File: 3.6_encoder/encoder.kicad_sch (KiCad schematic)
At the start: 3 parts, among them M1 Motor_Servo, SW1 RotaryEncoder_Switch, U1 ESP32-S3-DevKitC

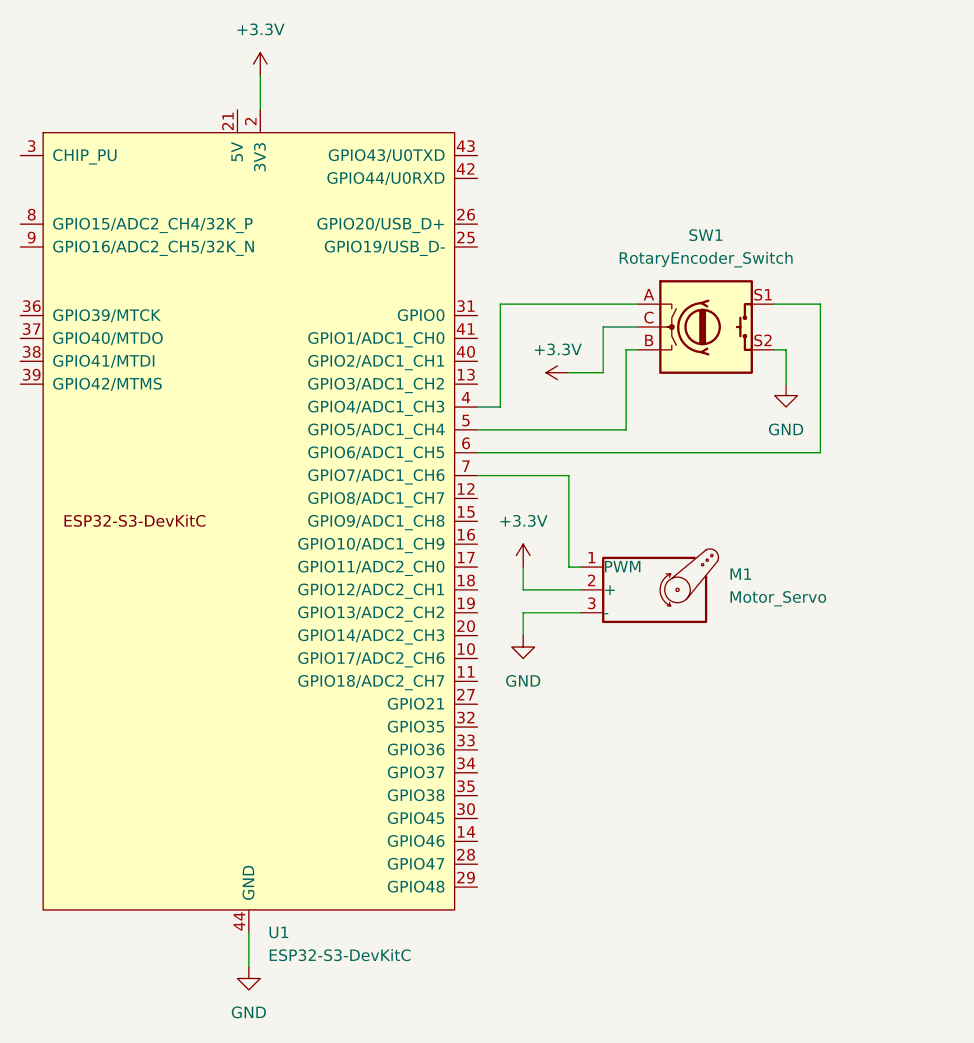
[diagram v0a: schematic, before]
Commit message: added parts for HW 3.6
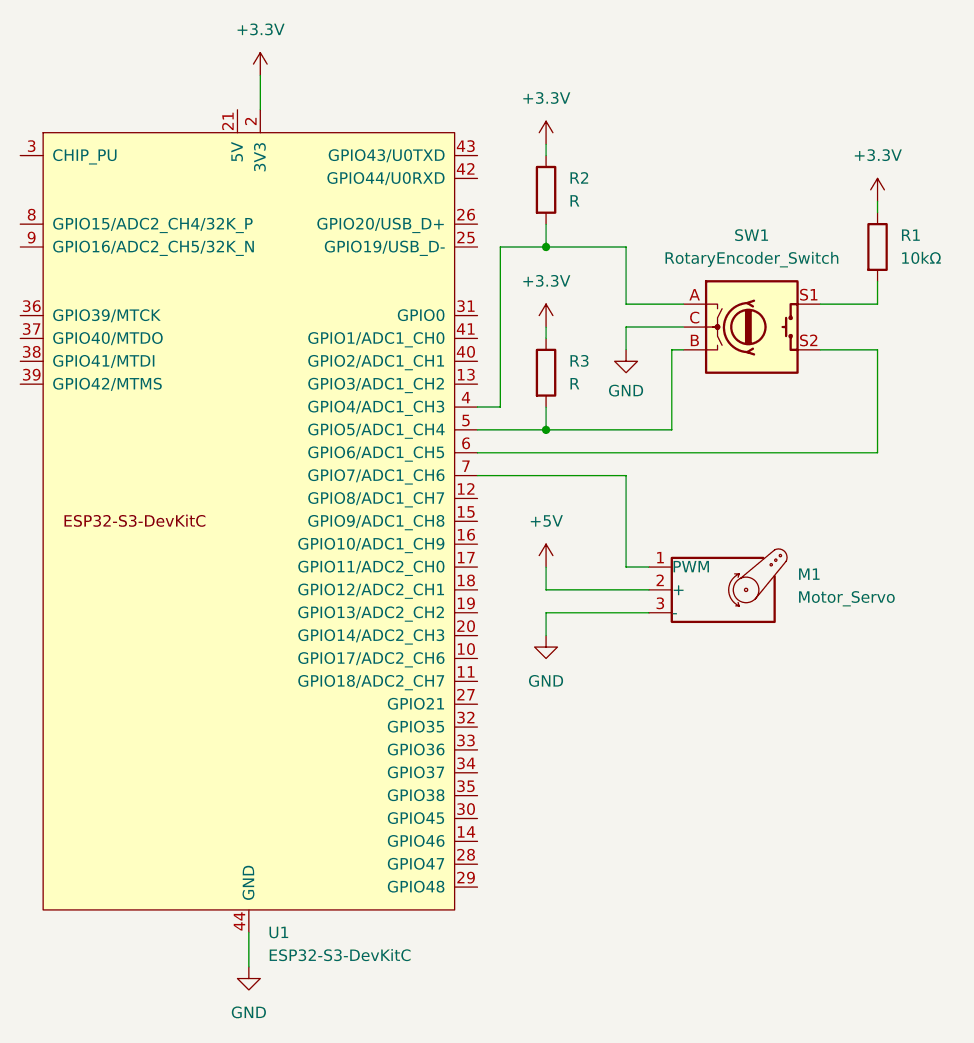
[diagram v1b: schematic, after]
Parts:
- added R1: 10kΩ, symbol Device:R
- added R2, R3: R, symbol Device:R
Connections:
- net +3.3V: now also R1.1, R2.1, R3.1; no longer M1.2 (+), SW1.C
- net GND: now also SW1.C; no longer SW1.S2
- net at SW1.A, U1.4 (GPIO4/ADC1_CH3): now also R2.2
- net at SW1.B, U1.5 (GPIO5/ADC1_CH4): now also R3.2
- net at SW1.S1: now also R1.2; no longer U1.6 (GPIO6/ADC1_CH5)
- new net: SW1.S2, U1.6 (GPIO6/ADC1_CH5)
- new net +5V: M1.2 (+)
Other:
- moved on the sheet: M1, SW1
